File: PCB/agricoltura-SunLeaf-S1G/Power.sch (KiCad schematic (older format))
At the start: 17 parts, among them Q1 DMP3125L-7, Q2 DMP3125L-7, T4 B2B-PH-K-S(LF)(SN), T5 B3B-PH-K-S(LF)(SN), U2 BQ24210DQCT, U3 AZ1117CR-3.3TRG1

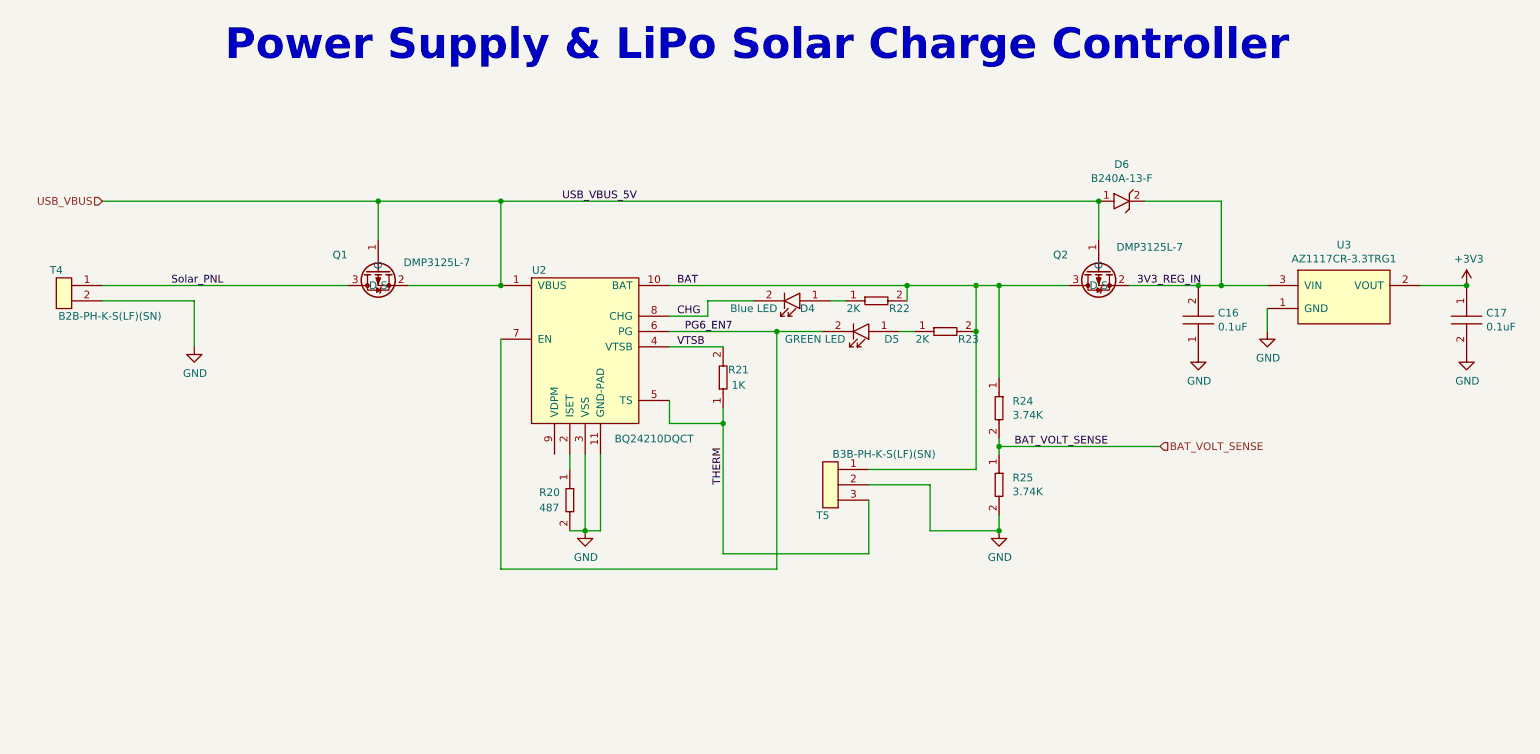
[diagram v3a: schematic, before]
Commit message: Pullups
Added pullup reistors to I2C ports, changed JTAG connector over to Tag connect.
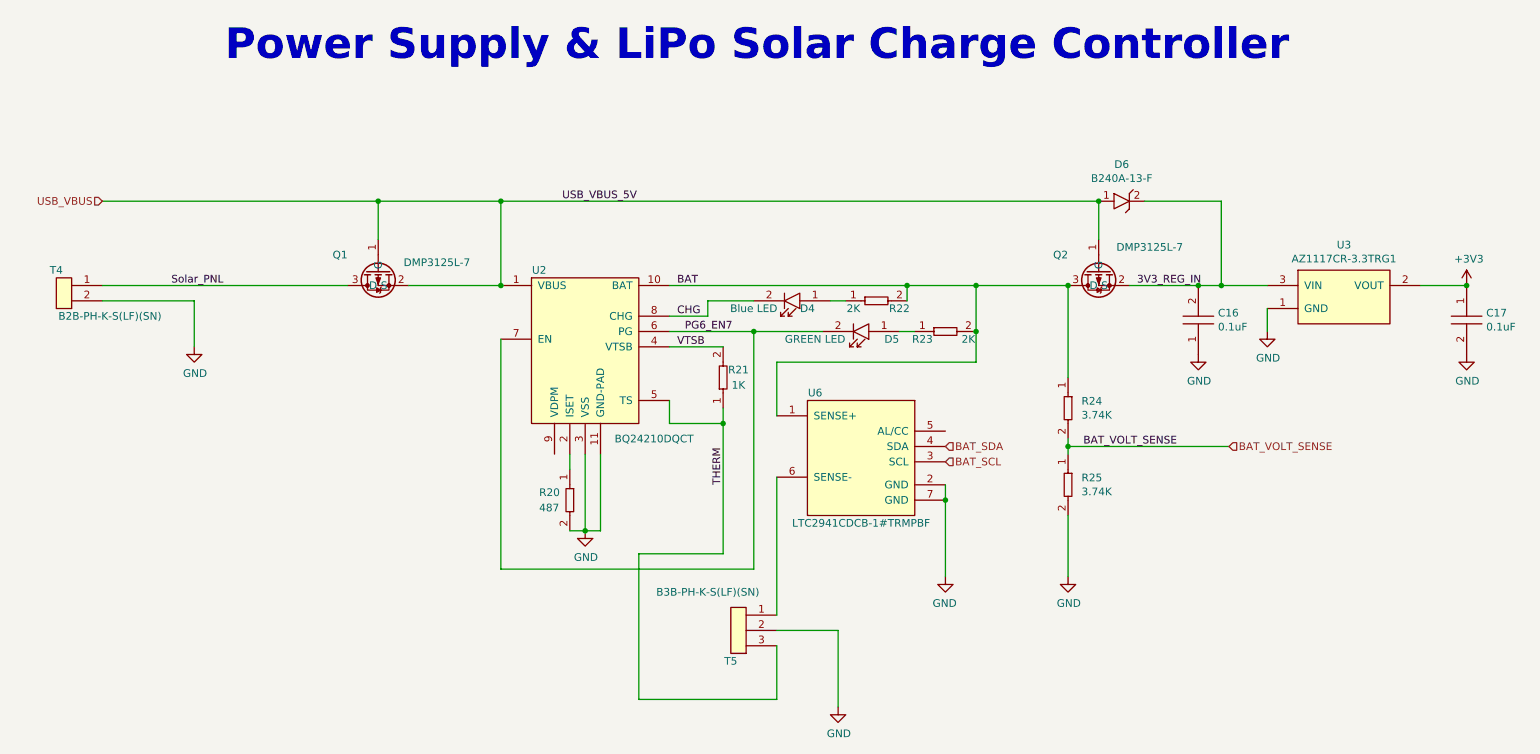
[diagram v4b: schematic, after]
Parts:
- added U6: LTC2941CDCB-1#TRMPBF, AVR-KiCAD-Lib-ICs:LTC2941CDCB-1-TRMPBF, symbol AVR-KiCAD-Lib-ICs:LTC2941CDCB-1#TRMPBF
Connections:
- net BAT: now also U6.1 (SENSE+); no longer T5.1
- net GND: now also U6.2 (GND), U6.7 (GND)
- new net: T5.1, U6.6 (SENSE-)
- new net BAT_SCL: U6.3 (SCL)
- new net BAT_SDA: U6.4 (SDA)
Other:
- moved on the sheet: R24, R25, T5

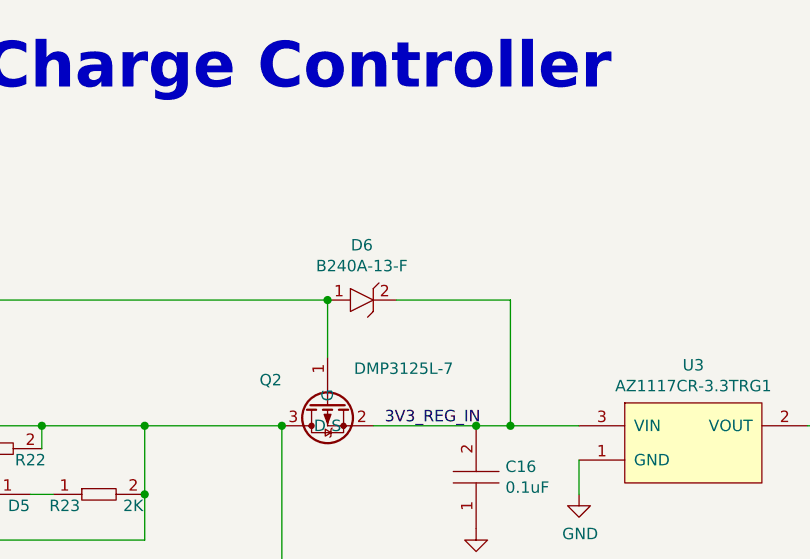
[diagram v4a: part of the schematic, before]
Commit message: Routing Complete
Board routing completed, also added EEPROM for storing configuration settings.
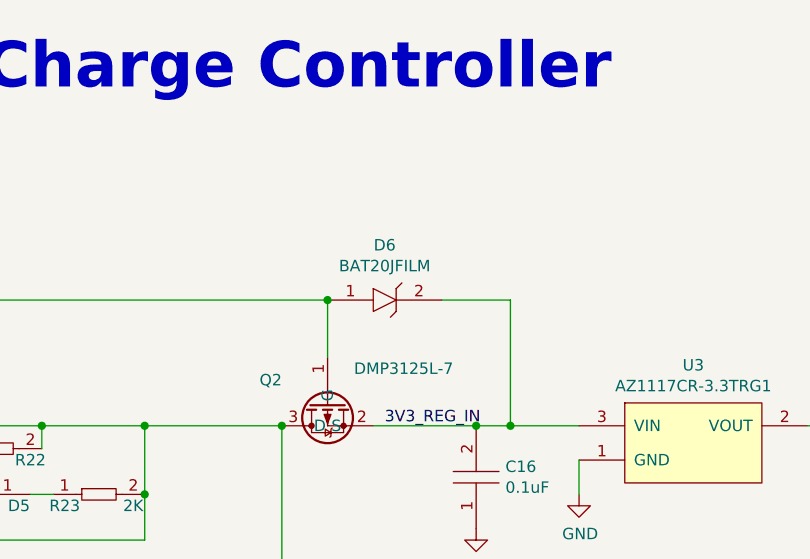
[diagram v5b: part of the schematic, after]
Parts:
- removed D6: B240A-13-F, AVR-KiCAD-Lib-Diodes:B240A-13-F, symbol AVR-KiCAD-Lib-Diodes:B240A-13-F
- added D6: BAT20JFILM, AVR-KiCAD-Lib-Diodes:BAT20JFILM, symbol AVR-KiCAD-Lib-Diodes:BAT20JFILM
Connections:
- net 3V3_REG_IN: now also D6.2
- net USB_VBUS: now also D6.1
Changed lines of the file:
@@
 Wire Wire Line
 	3500 3450 3500 3200
-Connection ~ 8200 3200
 Wire Wire Line
 	8200 3200 4300 3200
@@
 Wire Wire Line
 	9000 3200 9000 3750
-Wire Wire Line
-	8500 3200 9000 3200
-$Comp
-L AVR-KiCAD-Lib-Diodes:B240A-13-F D6
-U 1 1 5F1169F4
-P 8350 3200
-F 0 "D6" H 8350 3440 50  0000 C CNN
-F 1 "B240A-13-F" H 8400 3400 50  0001 C CNN
-F 2 "AVR-KiCAD-Lib-Diodes:B240A-13-F" H 8100 3350 50  0001 C CNN
-F 3 "https://www.diodes.com/assets/Datasheets/ds13004.pdf" H 8250 3300 50  0001 C CNN
-F 4 "0.41000" H 8450 3450 50  0001 C CNN "Cost QTY: 1"
-F 5 "0.10100" H 8550 3550 50  0001 C CNN "Cost QTY: 1000"
-F 6 "0.09242" H 8650 3650 50  0001 C CNN "Cost QTY: 2500"
-F 7 "0.08838" H 8750 3750 50  0001 C CNN "Cost QTY: 5000"
-F 8 "0.07828" H 8850 3850 50  0001 C CNN "Cost QTY: 10000"
-F 9 "Diodes Incorporated" H 8950 3950 50  0001 C CNN "MFR"
-F 10 "B240A-13-F" H 9050 4050 50  0001 C CNN "MFR#"
-F 11 "Digikey" H 9150 4150 50  0001 C CNN "Vendor"
-F 12 "B240A-FDICT-ND" H 9250 4250 50  0001 C CNN "Vendor #"
-F 13 "AVR" H 9350 4350 50  0001 C CNN "Designer"
-F 14 "0.73mm" H 9450 4450 50  0001 C CNN "Height"
-F 15 "3/30/2020" H 10550 5550 50  0001 C CNN "Date Created"
-F 16 "3/30/2020" H 9550 4550 50  0001 C CNN "Date Modified"
-F 17 "Yes" H 9650 4650 50  0001 C CNN "Lead-Free ?"
-F 18 "1" H 9750 4750 50  0001 C CNN "RoHS Levels"
-F 19 "SMT" H 9850 4850 50  0001 C CNN "Mounting"
-F 20 "2" H 9950 4950 50  0001 C CNN "Pin Count #"
-F 21 "Active" H 10050 5050 50  0001 C CNN "Status"
-F 22 "*" H 10150 5150 50  0001 C CNN "Tolerance"
-F 23 "TVS Diode" H 10250 5250 50  0001 C CNN "Type"
-F 24 "40V" H 10350 5350 50  0001 C CNN "Voltage"
-F 25 "DO-214AC, SMA" H 10450 5500 50  0001 C CNN "Package"
-F 26 "Diode Schottky 40V 2A Surface Mount SMA" H 10750 5800 50  0001 C CNN "Description"
-F 27 "B240A-13-F" H 8350 3349 50  0000 C CNN "_Value_"
-F 28 "*" H 10750 5800 50  0001 C CNN "Management_ID"
-	1    8350 3200
-	1    0    0    -1
-$EndComp
 Wire Wire Line
 	1700 3750 3300 3750
@@
 Text HLabel 7200 4900 2    50   Input ~ 0
 BAT_SCL
+$Comp
+L AVR-KiCAD-Lib-Diodes:BAT20JFILM D6
+U 1 1 5F31DBDB
+P 8450 3200
+F 0 "D6" H 8450 3440 50  0000 C CNN
+F 1 "BAT20JFILM" H 8500 3400 50  0001 C CNN
+F 2 "AVR-KiCAD-Lib-Diodes:BAT20JFILM" H 8350 3200 50  0001 C CNN
+F 3 "https://www.st.com/content/ccc/resource/technical/document/datasheet/group1/81/a4/1f/0e/ca/8c/47/ba/CD00012201/files/CD00012201.pdf/jcr:content/translations/en.CD00012201.pdf" H 8350 3300 50  0001 C CNN
+F 4 "0.32000" H 8550 3450 50  0001 C CNN "Cost QTY: 1"
+F 5 "0.06120" H 8650 3550 50  0001 C CNN "Cost QTY: 1000"
+F 6 "*" H 8750 3650 50  0001 C CNN "Cost QTY: 2500"
+F 7 "*" H 8850 3750 50  0001 C CNN "Cost QTY: 5000"
+F 8 "*" H 8950 3850 50  0001 C CNN "Cost QTY: 10000"
+F 9 "STMicroelectronics" H 9050 3950 50  0001 C CNN "MFR"
+F 10 "BAT20JFILM" H 9150 4050 50  0001 C CNN "MFR#"
+F 11 "Digikey" H 9250 4150 50  0001 C CNN "Vendor"
+F 12 "497-3381-1-ND" H 9350 4250 50  0001 C CNN "Vendor #"
+F 13 "AVR" H 9450 4350 50  0001 C CNN "Designer"
+F 14 "1.13mm" H 9550 4450 50  0001 C CNN "Height"
+F 15 "7/19/2020" H 10650 5550 50  0001 C CNN "Date Created"
+F 16 "7/19/2020" H 9650 4550 50  0001 C CNN "Date Modified"
+F 17 "Yes" H 9750 4650 50  0001 C CNN "Lead-Free ?"
+F 18 "1" H 9850 4750 50  0001 C CNN "RoHS Levels"
+F 19 "SMT" H 9950 4850 50  0001 C CNN "Mounting"
+F 20 "2" H 10050 4950 50  0001 C CNN "Pin Count #"
+F 21 "Active" H 10150 5050 50  0001 C CNN "Status"
+F 22 "*" H 10250 5150 50  0001 C CNN "Tolerance"
+F 23 "Schottky Diode" H 10350 5250 50  0001 C CNN "Type"
+F 24 "23V" H 10450 5350 50  0001 C CNN "Voltage"
+F 25 "SOD-323" H 10550 5500 50  0001 C CNN "Package"
+F 26 "Diode Schottky 23V 1A Surface Mount SOD-323" H 10850 5800 50  0001 C CNN "Description"
+F 27 "BAT20JFILM" H 8450 3349 50  0000 C CNN "_Value_"
+F 28 "*" H 10850 5800 50  0001 C CNN "Management_ID"
+	1    8450 3200
+	1    0    0    -1
+$EndComp
+Connection ~ 8200 3200
+Wire Wire Line
+	8700 3200 9000 3200
 $EndSCHEMATC
